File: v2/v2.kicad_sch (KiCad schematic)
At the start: 71 parts, among them J1 rBUSoutV, J10 mcuTIEout, J11 USB_C_Receptacle_USB2.0, J12 Conn_01x06_Female, J2 rBUSinV, J3 cTIEoutV, J4 cTIEinV, J5 cBUSoutH, J6 rTIEoutH, J7 mcuTIEin, J8 rTIEinH, J9 cBUSinH, SW1 KeySwitch, SW10 KeySwitch, SW11 KeySwitch, SW12 KeySwitch, SW13 KeySwitch, SW14 KeySwitch, SW15 KeySwitch, SW16 KeySwitch, SW17 KeySwitch, SW18 KeySwitch, SW19 KeySwitch, SW2 KeySwitch, SW20 KeySwitch, SW21 KeySwitch, SW22 KeySwitch, SW23 KeySwitch, SW24 KeySwitch, SW25 KeySwitch, SW3 KeySwitch, SW4 KeySwitch, SW5 KeySwitch, SW6 KeySwitch, SW7 KeySwitch, SW8 KeySwitch, SW9 KeySwitch, U1 ItsyBitsy5V

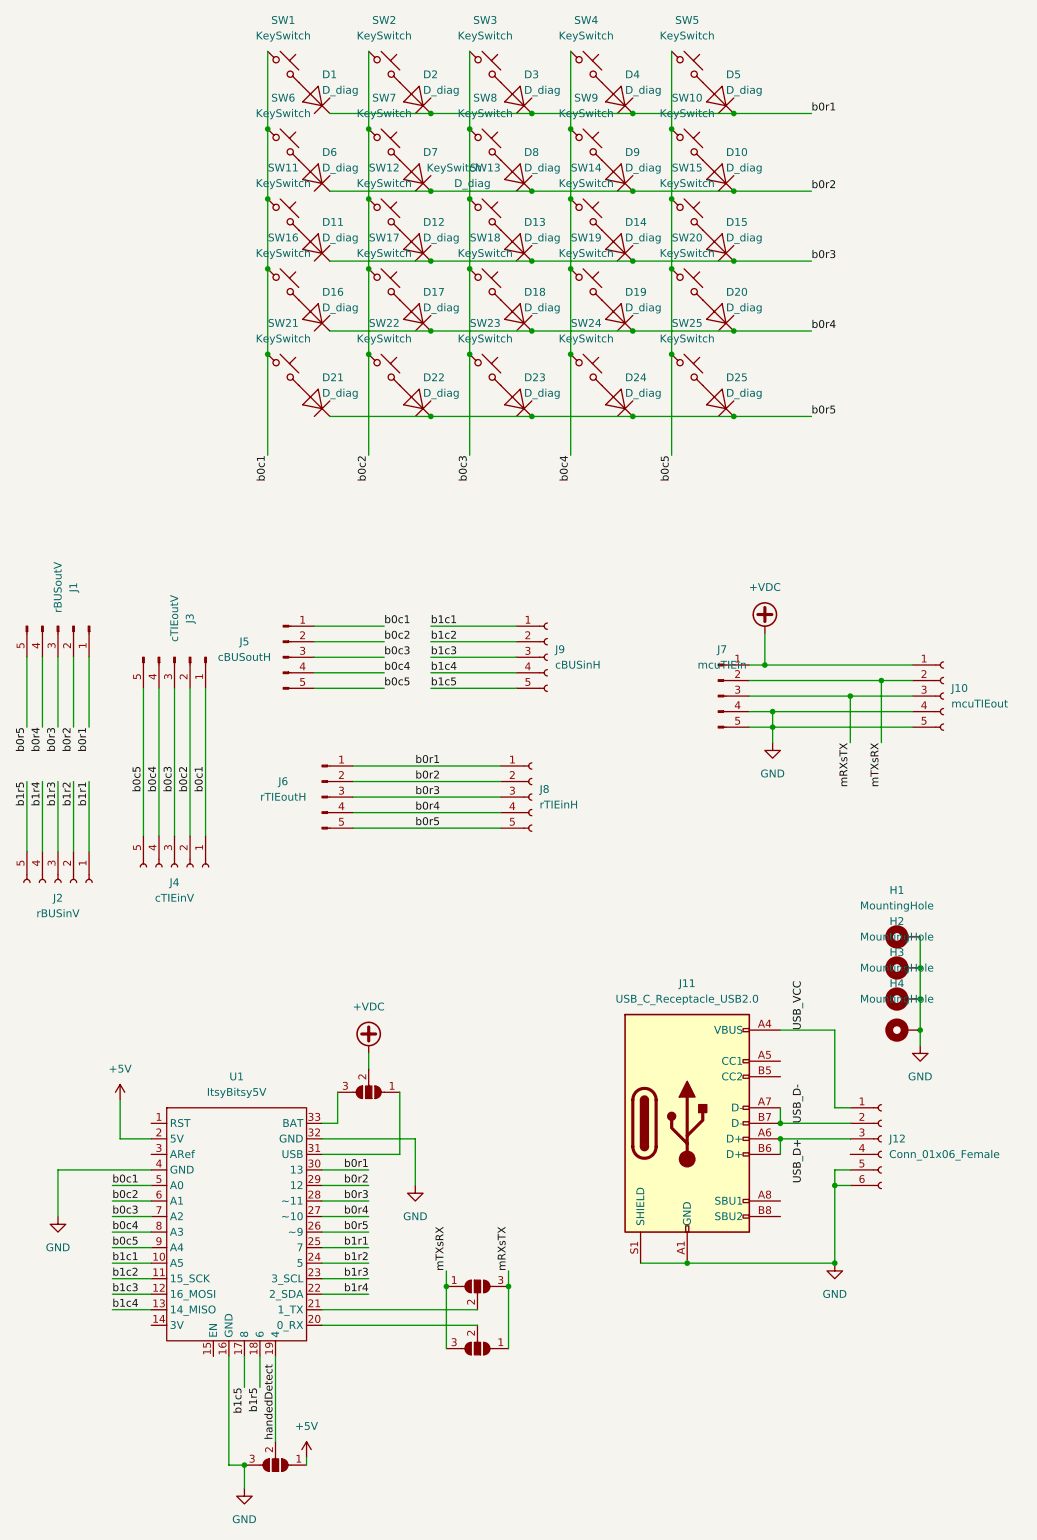
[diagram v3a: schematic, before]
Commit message: Optimise and reroute after first order feedback. Also add ordered files archive.
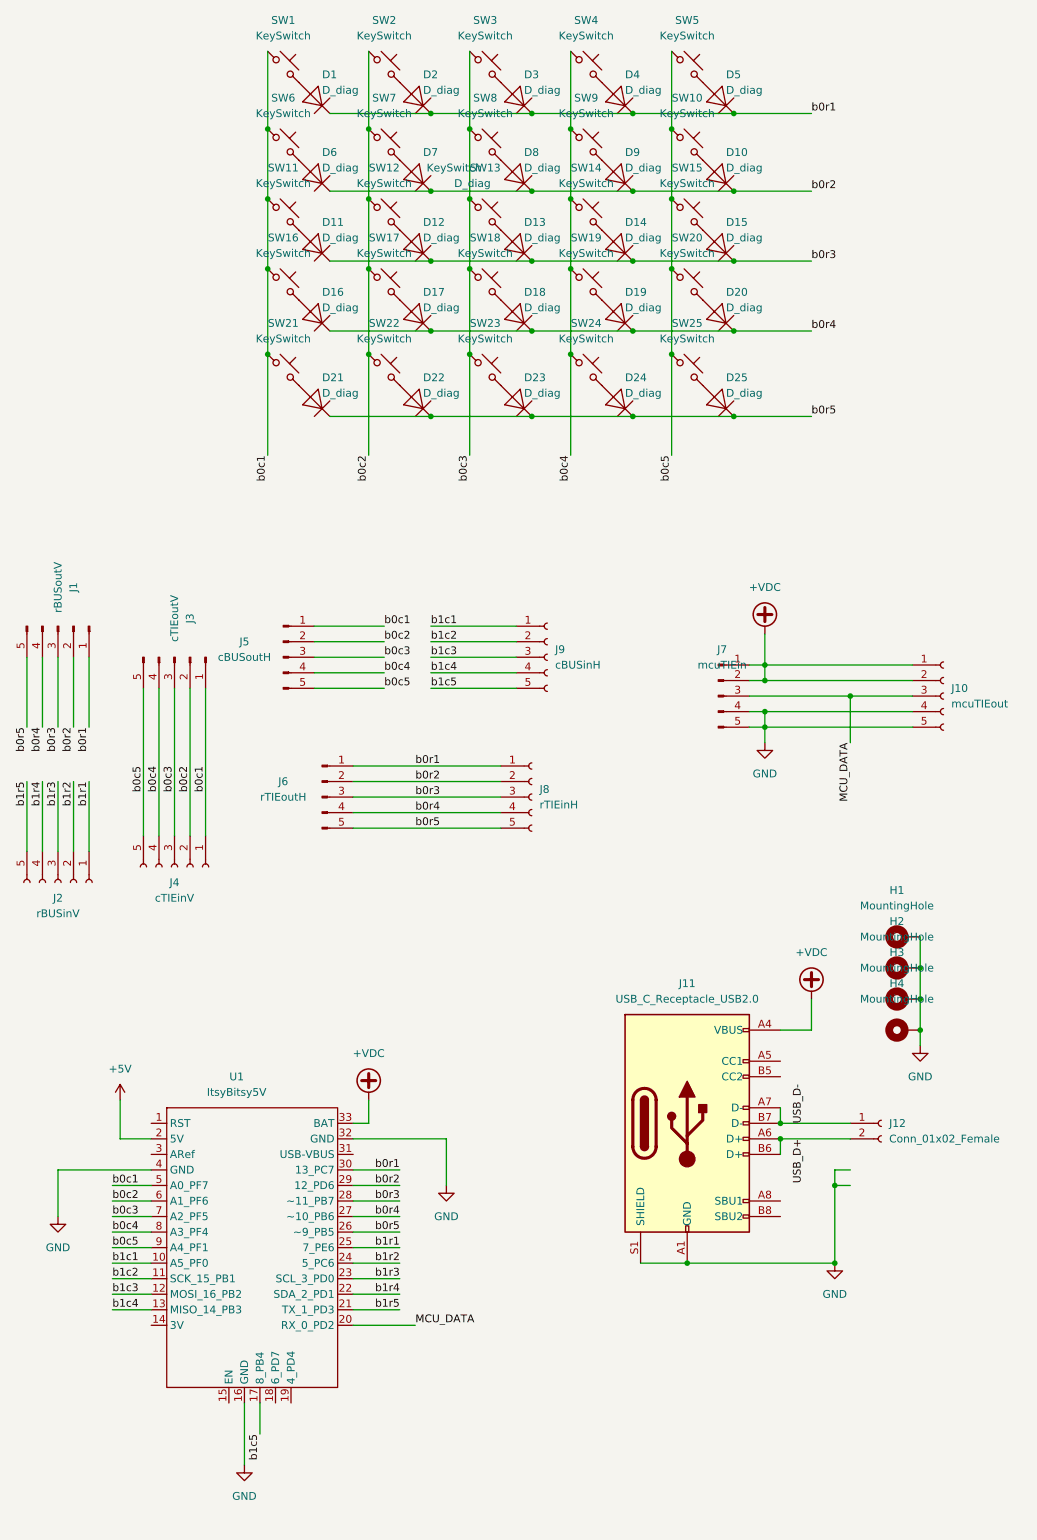
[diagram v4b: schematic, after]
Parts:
- removed J12: Conn_01x06_Female, ProjectLibrary:USB_JUMP_PAD, symbol Connector:Conn_01x06_Female
- removed JP1, JP2, JP3, JP4: SolderJumper_3_Open, ProjectLibrary:SolderJumper-3_P1.3mm_Open_RoundedPad1.0x1.5mm_No_Silk, symbol Jumper:SolderJumper_3_Open
- added J12: Conn_01x02_Female, ProjectLibrary:USB_JUMP_PAD, symbol Connector:Conn_01x02_Female
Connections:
- net USB_VCC is gone; now on net +VDC: J11.A4 (VBUS), J11.A9 (VBUS), J11.B4 (VBUS), J11.B9 (VBUS)
- net mRXsTX is gone; now on net MCU_DATA: J10.3 (Pin_3), J7.3 (Pin_3)
- net mTXsRX is gone; now on net +VDC: J10.2 (Pin_2), J7.2 (Pin_2)
- net +VDC: now also U1.33 (BAT)
- net USB_D+: now also J12.2 (Pin_2)
- net USB_D-: now also J12.1 (Pin_1)
- net b1r5: now also U1.21 (TX_1_PD3); no longer U1.18 (6)
- net MCU_DATA: now reaches U1.20 (RX_0_PD2)
- net handedDetect: no longer names the net of U1.19 (4_PD4)
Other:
- moved on the sheet: U1
